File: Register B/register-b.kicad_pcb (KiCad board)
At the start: 2 copper layers, 78.7 x 58.4 mm, 50 parts, among them J1 Bus, J2 Address, J3 Conn_01x04_Male, J4 Power, U1 74LS245, U2 74LS173, U3 74LS173

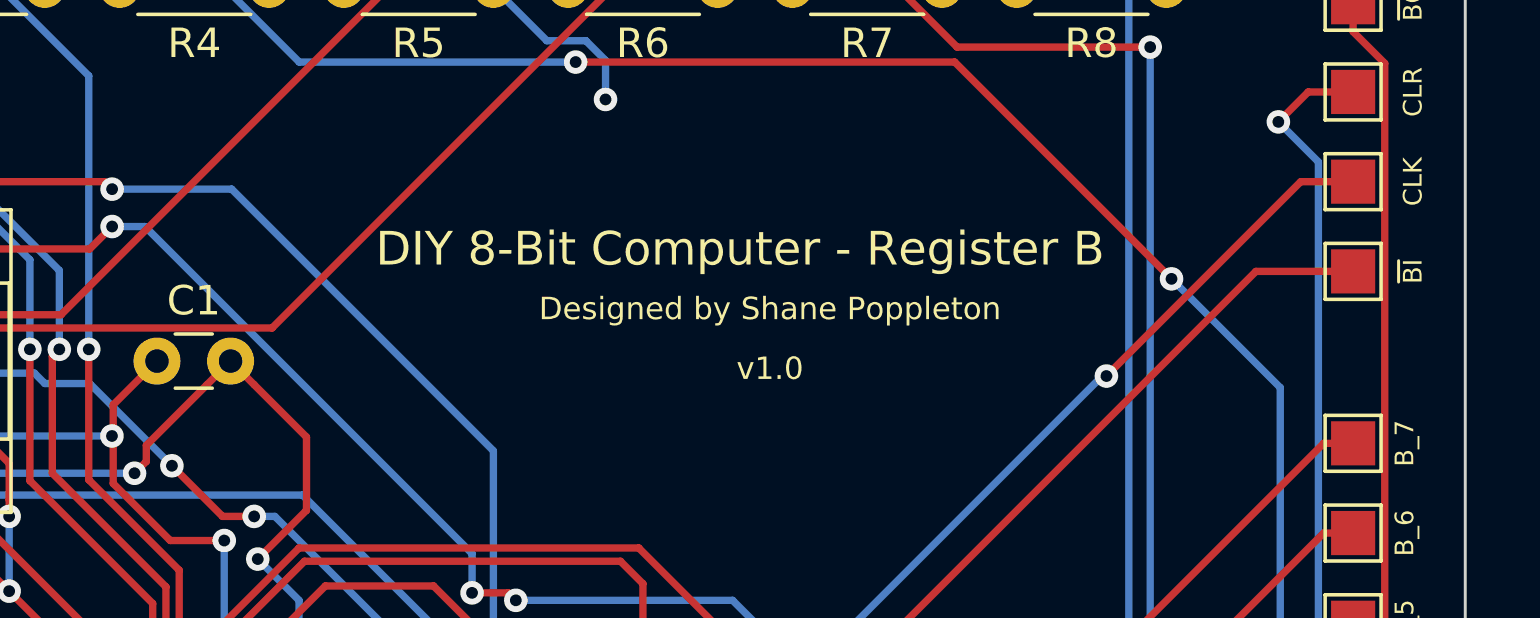
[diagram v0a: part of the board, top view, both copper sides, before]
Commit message: Added Attribution on each PCB, and regenerated gerbers
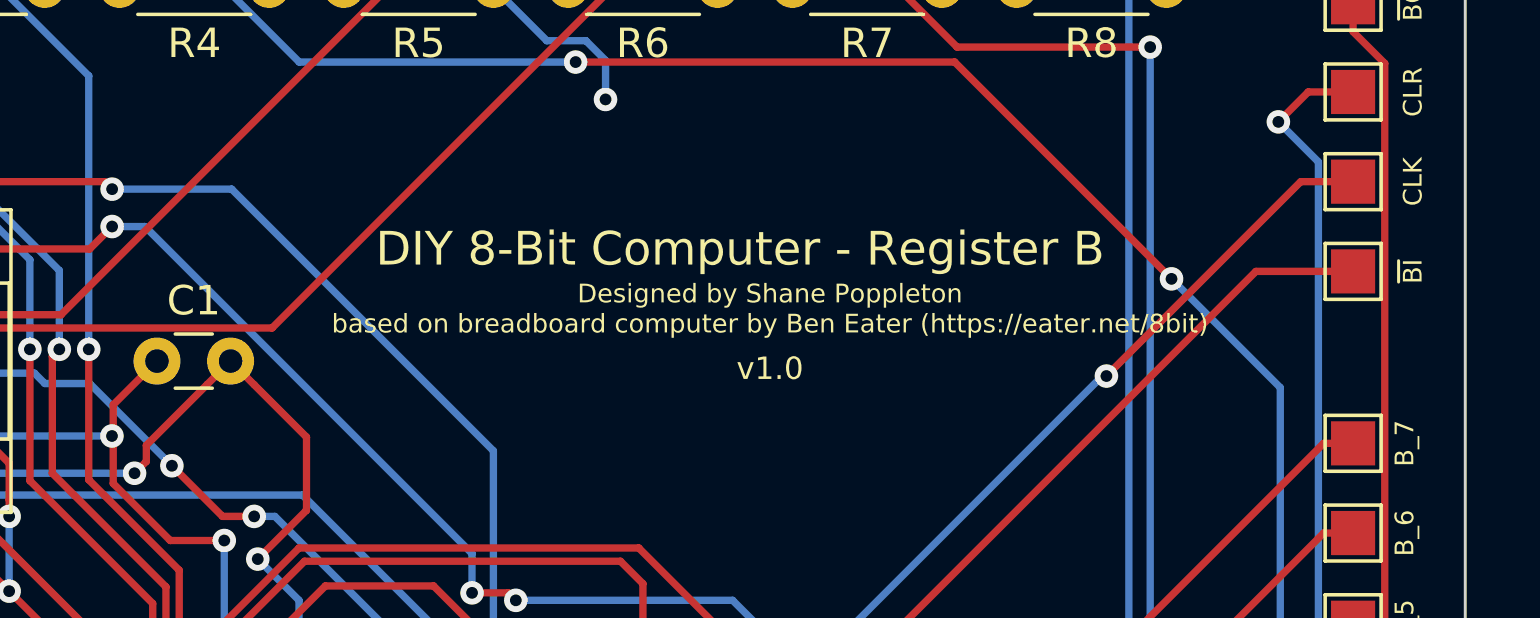
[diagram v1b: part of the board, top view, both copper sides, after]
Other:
- board text added: "Designed by Shane Poppleton based on breadboard computer by Ben Eater (https://eater.net/8bit)"
- board text removed: "Designed by Shane Poppleton"
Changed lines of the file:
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@@
     (effects (font (size 0.762 0.762) (thickness 0.127)))
   )
-  (gr_text "Designed by Shane Poppleton" (at 70.358 49.022) (layer F.SilkS)
-    (effects (font (size 0.762 0.762) (thickness 0.127)))
+  (gr_text "Designed by Shane Poppleton\nbased on breadboard computer by Ben Eater (https://eater.net/8bit)\n" (at 70.358 49.022) (layer F.SilkS)
+    (effects (font (size 0.635 0.635) (thickness 0.1016)))
   )
   (gr_text "DIY 8-Bit Computer - Register B" (at 69.342 46.99) (layer F.SilkS)
@@
   (segment (start 53.993999 62.629999) (end 54.210001 62.629999) (width 0.25) (layer F.Cu) (net 1))
   (segment (start 53.594 62.23) (end 53.993999 62.629999) (width 0.25) (layer F.Cu) (net 1))
+  (via (at 82.925 78.486) (size 0.8) (drill 0.4) (layers F.Cu B.Cu) (net 1))
+  (segment (start 77.724 78.486) (end 82.925 78.486) (width 0.25) (layer B.Cu) (net 1))
+  (segment (start 76.2 80.01) (end 77.724 78.486) (width 0.25) (layer B.Cu) (net 1))
+  (segment (start 90.17 39.608) (end 90.17 38.608) (width 0.25) (layer F.Cu) (net 1))
+  (segment (start 91.245001 63.748001) (end 91.245001 40.683001) (width 0.25) (layer F.Cu) (net 1))
+  (segment (start 91.180001 63.813001) (end 91.245001 63.748001) (width 0.25) (layer F.Cu) (net 1))
+  (segment (start 90.057997 63.813001) (end 91.180001 63.813001) (width 0.25) (layer F.Cu) (net 1))
+  (segment (start 91.245001 40.683001) (end 90.17 39.608) (width 0.25) (layer F.Cu) (net 1))
+  (segment (start 82.925 70.945998) (end 90.057997 63.813001) (width 0.25) (layer F.Cu) (net 1))
+  (segment (start 82.925 78.486) (end 82.925 70.945998) (width 0.25) (layer F.Cu) (net 1))
+  (segment (start 76.2 80.01) (end 74.93 81.28) (width 0.25) (layer B.Cu) (net 1))
+  (segment (start 74.93 81.28) (end 25.146 81.28) (width 0.25) (layer B.Cu) (net 1))
+  (segment (start 25.146 81.28) (end 23.876 80.01) (width 0.25) (layer B.Cu) (net 1))
+  (segment (start 23.876 80.01) (end 23.876 76.2) (width 0.25) (layer B.Cu) (net 1))
+  (segment (start 23.876 76.2) (end 26.814999 73.261001) (width 0.25) (layer B.Cu) (net 1))
+  (segment (start 26.814999 62.085001) (end 27.94 60.96) (width 0.25) (layer B.Cu) (net 1))
+  (segment (start 26.814999 73.261001) (end 26.814999 62.085001) (width 0.25) (layer B.Cu) (net 1))
   (via (at 68.58 71.12) (size 0.8) (drill 0.4) (layers F.Cu B.Cu) (net 2))
   (segment (start 67.31 72.39) (end 68.58 71.12) (width 0.25) (layer F.Cu) (net 2))
@@
   (segment (start 38.1 56.115004) (end 38.1 55.74137) (width 0.25) (layer B.Cu) (net 28))
   (segment (start 45.72 68.58) (end 41.765001 64.625001) (width 0.25) (layer B.Cu) (net 28))
-  (via (at 82.925 78.486) (size 0.8) (drill 0.4) (layers F.Cu B.Cu) (net 1))
-  (segment (start 77.724 78.486) (end 82.925 78.486) (width 0.25) (layer B.Cu) (net 1))
-  (segment (start 76.2 80.01) (end 77.724 78.486) (width 0.25) (layer B.Cu) (net 1))
-  (segment (start 90.17 39.608) (end 90.17 38.608) (width 0.25) (layer F.Cu) (net 1))
-  (segment (start 91.245001 63.748001) (end 91.245001 40.683001) (width 0.25) (layer F.Cu) (net 1))
-  (segment (start 91.180001 63.813001) (end 91.245001 63.748001) (width 0.25) (layer F.Cu) (net 1))
-  (segment (start 90.057997 63.813001) (end 91.180001 63.813001) (width 0.25) (layer F.Cu) (net 1))
-  (segment (start 91.245001 40.683001) (end 90.17 39.608) (width 0.25) (layer F.Cu) (net 1))
-  (segment (start 82.925 70.945998) (end 90.057997 63.813001) (width 0.25) (layer F.Cu) (net 1))
-  (segment (start 82.925 78.486) (end 82.925 70.945998) (width 0.25) (layer F.Cu) (net 1))
-  (segment (start 76.2 80.01) (end 74.93 81.28) (width 0.25) (layer B.Cu) (net 1))
-  (segment (start 74.93 81.28) (end 25.146 81.28) (width 0.25) (layer B.Cu) (net 1))
-  (segment (start 25.146 81.28) (end 23.876 80.01) (width 0.25) (layer B.Cu) (net 1))
-  (segment (start 23.876 80.01) (end 23.876 76.2) (width 0.25) (layer B.Cu) (net 1))
-  (segment (start 23.876 76.2) (end 26.814999 73.261001) (width 0.25) (layer B.Cu) (net 1))
-  (segment (start 26.814999 62.085001) (end 27.94 60.96) (width 0.25) (layer B.Cu) (net 1))
-  (segment (start 26.814999 73.261001) (end 26.814999 62.085001) (width 0.25) (layer B.Cu) (net 1))
   (via (at 74.93 64.160031) (size 0.8) (drill 0.4) (layers F.Cu B.Cu) (net 29))
   (segment (start 73.66 62.890031) (end 74.93 64.160031) (width 0.25) (layer B.Cu) (net 29))
